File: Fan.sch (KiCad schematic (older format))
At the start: 9 parts

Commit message: Added Arduino and top-level connections
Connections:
- net labels added: CURR_MEAS, FAN_EN_N, FAN_OUT+, FAN_OUT-, TACH_IN, TACH_MEAS
- net labels removed: Current_Measure, Fan_in, Power+, Power-, Tach, Tach_out
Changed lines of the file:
@@
 $Descr A4 11693 8268
 encoding utf-8
-Sheet 7 9
+Sheet 8 9
 Title ""
 Date ""
@@
 $EndDescr
 Text HLabel 8800 3400 0    60   Output ~ 0
-Power+
-Text HLabel 8800 3600 0    60   Input ~ 0
-Power-
+FAN_OUT+
+Text HLabel 8800 3600 0    60   Output ~ 0
+FAN_OUT-
 Text HLabel 8800 4000 0    60   Input ~ 0
-Tach
+TACH_IN
 Text HLabel 1500 5300 0    60   Output ~ 0
-Tach_out
+TACH_MEAS
 Text HLabel 1500 4700 0    60   Input ~ 0
-Fan_in
+FAN_EN_N
 $Comp
 L LM324 U?
@@
 	7800 5300 1500 5300
 Text HLabel 1500 5000 0    60   Output ~ 0
-Current_Measure
+CURR_MEAS
 Wire Wire Line
 	7200 3900 6600 3900

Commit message: Current/fan driver circuit reworked
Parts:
- removed R? (x3): R, symbol R
- removed RV?: POT, symbol POT
- added D?: DIODE, symbol DIODE
- added Q? (x2): MOSFET_N, symbol MOSFET_N
- added TH?: THERMISTOR, symbol THERMISTOR
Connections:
- net labels added: +12C, FAN_MODE, FAN_PWM
- net labels removed: FAN_EN_N
- wire segments 36 -> 34
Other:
- moved on the sheet: R?
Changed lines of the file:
@@
 $Descr A4 11693 8268
 encoding utf-8
-Sheet 8 9
+Sheet 7 9
 Title ""
 Date ""
@@
 Comment4 ""
 $EndDescr
-Text HLabel 8800 3400 0    60   Output ~ 0
+Text HLabel 10500 1700 2    60   Output ~ 0
 FAN_OUT+
-Text HLabel 8800 3600 0    60   Output ~ 0
+Text HLabel 10500 1900 2    60   Output ~ 0
 FAN_OUT-
-Text HLabel 8800 4000 0    60   Input ~ 0
+Text HLabel 10500 6100 2    60   Input ~ 0
 TACH_IN
-Text HLabel 1500 5300 0    60   Output ~ 0
+Text HLabel 1500 6100 0    60   Output ~ 0
 TACH_MEAS
-Text HLabel 1500 4700 0    60   Input ~ 0
-FAN_EN_N
+Text HLabel 1500 3600 0    60   Input ~ 0
+FAN_PWM
 $Comp
 L LM324 U?
@@
 $EndComp
 $Comp
-L +12V #PWR?
-U 1 1 52F02708
-P 7200 2000
-F 0 "#PWR?" H 7200 1950 20  0001 C CNN
-F 1 "+12V" H 7200 2100 30  0000 C CNN
-F 2 "" H 7200 2000 60  0000 C CNN
-F 3 "" H 7200 2000 60  0000 C CNN
-	1    7200 2000
-	1    0    0    -1
-$EndComp
-Wire Wire Line
-	7200 2000 7200 2400
-Wire Wire Line
-	7200 2800 7200 3400
-Wire Wire Line
-	7200 3400 8800 3400
-Wire Wire Line
-	5100 3600 7200 3600
-Wire Wire Line
-	7200 3600 8800 3600
-Wire Wire Line
-	7200 3600 7200 3900
-Wire Wire Line
-	7200 3900 7200 4100
-$Comp
 L R R?
 U 1 1 52F02733
-P 7200 4350
-F 0 "R?" V 7280 4350 40  0000 C CNN
-F 1 "R" V 7207 4351 40  0000 C CNN
-F 2 "" V 7130 4350 30  0000 C CNN
-F 3 "" H 7200 4350 30  0000 C CNN
-	1    7200 4350
+P 7200 5050
+F 0 "R?" V 7280 5050 40  0000 C CNN
+F 1 "R" V 7207 5051 40  0000 C CNN
+F 2 "" V 7130 5050 30  0000 C CNN
+F 3 "" H 7200 5050 30  0000 C CNN
+	1    7200 5050
 	1    0    0    -1
 $EndComp
@@
 L AGND #PWR?
 U 1 1 52F02747
-P 7200 5000
-F 0 "#PWR?" H 7200 5000 40  0001 C CNN
-F 1 "AGND" H 7200 4930 50  0000 C CNN
-F 2 "" H 7200 5000 60  0000 C CNN
-F 3 "" H 7200 5000 60  0000 C CNN
-	1    7200 5000
-	1    0    0    -1
-$EndComp
-Wire Wire Line
-	7200 4600 7200 5000
-Wire Wire Line
-	6400 2600 6900 2600
+P 7200 5700
+F 0 "#PWR?" H 7200 5700 40  0001 C CNN
+F 1 "AGND" H 7200 5630 50  0000 C CNN
+F 2 "" H 7200 5700 60  0000 C CNN
+F 3 "" H 7200 5700 60  0000 C CNN
+	1    7200 5700
+	1    0    0    -1
+$EndComp
 $Comp
 L +12V #PWR?
@@
 	1    0    0    -1
 $EndComp
-Wire Wire Line
-	5800 1900 5800 2200
 $Comp
 L -12V #PWR?
@@
 	-1   0    0    1
 $EndComp
-Wire Wire Line
-	5800 3250 5800 3000
-Wire Wire Line
-	5100 3600 5100 2700
-Wire Wire Line
-	5100 2700 5400 2700
-Connection ~ 7200 3600
-Wire Wire Line
-	3600 2500 3900 2500
-Wire Wire Line
-	3900 2500 4400 2500
-Wire Wire Line
-	4400 2500 5400 2500
-$Comp
-L R R?
-U 1 1 52F027CA
-P 3900 2050
-F 0 "R?" V 3980 2050 40  0000 C CNN
-F 1 "R" V 3907 2051 40  0000 C CNN
-F 2 "" V 3830 2050 30  0000 C CNN
-F 3 "" H 3900 2050 30  0000 C CNN
-	1    3900 2050
-	1    0    0    -1
-$EndComp
-Wire Wire Line
-	3900 2300 3900 2500
-Wire Wire Line
-	3900 2500 3900 2900
-$Comp
-L +12V #PWR?
-U 1 1 52F027E4
-P 3900 1500
-F 0 "#PWR?" H 3900 1450 20  0001 C CNN
-F 1 "+12V" H 3900 1600 30  0000 C CNN
-F 2 "" H 3900 1500 60  0000 C CNN
-F 3 "" H 3900 1500 60  0000 C CNN
-	1    3900 1500
-	1    0    0    -1
-$EndComp
-Wire Wire Line
-	3900 1500 3900 1800
-$Comp
-L POT RV?
-U 1 1 52F02801
-P 3900 3150
-F 0 "RV?" H 3900 3050 50  0000 C CNN
-F 1 "POT" H 3900 3150 50  0000 C CNN
-F 2 "" H 3900 3150 60  0000 C CNN
-F 3 "" H 3900 3150 60  0000 C CNN
-	1    3900 3150
-	0    -1   -1   0
-$EndComp
-Connection ~ 3900 2500
 $Comp
 L AGND #PWR?
 U 1 1 52F0282F
-P 3900 3700
-F 0 "#PWR?" H 3900 3700 40  0001 C CNN
-F 1 "AGND" H 3900 3630 50  0000 C CNN
-F 2 "" H 3900 3700 60  0000 C CNN
-F 3 "" H 3900 3700 60  0000 C CNN
-	1    3900 3700
-	1    0    0    -1
-$EndComp
-Wire Wire Line
-	3900 3700 3900 3400
+P 4600 3400
+F 0 "#PWR?" H 4600 3400 40  0001 C CNN
+F 1 "AGND" H 4600 3330 50  0000 C CNN
+F 2 "" H 4600 3400 60  0000 C CNN
+F 3 "" H 4600 3400 60  0000 C CNN
+	1    4600 3400
+	1    0    0    -1
+$EndComp
 $Comp
 L MCP4922-E/P U?
@@
 	1    0    0    -1
 $EndComp
-Wire Wire Line
-	8800 4000 7800 4000
-Wire Wire Line
-	7800 4000 7800 5300
-Wire Wire Line
-	7800 5300 1500 5300
-Text HLabel 1500 5000 0    60   Output ~ 0
+Text HLabel 1500 4400 0    60   Output ~ 0
 CURR_MEAS
-Wire Wire Line
-	7200 3900 6600 3900
-Wire Wire Line
-	6600 3900 6600 5000
-Wire Wire Line
-	6600 5000 1500 5000
-Connection ~ 7200 3900
-$Comp
-L R R?
-U 1 1 52F0289B
-P 4400 3150
-F 0 "R?" V 4480 3150 40  0000 C CNN
-F 1 "R" V 4407 3151 40  0000 C CNN
-F 2 "" V 4330 3150 30  0000 C CNN
-F 3 "" H 4400 3150 30  0000 C CNN
-	1    4400 3150
-	1    0    0    -1
-$EndComp
-Wire Wire Line
-	4400 2900 4400 2500
-Connection ~ 4400 2500
-Wire Wire Line
-	4400 3400 4400 4700
-Wire Wire Line
-	4400 4700 1800 4700
-Wire Wire Line
-	1800 4700 1500 4700
 $Comp
 L R R?
@@
 Text HLabel 1500 2450 0    60   Input ~ 0
 MOSI
-Text HLabel 1500 3100 0    60   Output ~ 0
+Text HLabel 1450 2750 0    60   Output ~ 0
 MISO
 Text HLabel 1500 2650 0    60   Input ~ 0
@@
 Text HLabel 1500 2550 0    60   Input ~ 0
 SCLK
+$Comp
+L MOSFET_N Q?
+U 1 1 52FBE00D
+P 6600 5000
+F 0 "Q?" H 6610 5170 60  0000 R CNN
+F 1 "MOSFET_N" H 6610 4850 60  0000 R CNN
+F 2 "" H 6600 5000 60  0000 C CNN
+F 3 "" H 6600 5000 60  0000 C CNN
+	1    6600 5000
+	1    0    0    -1
+$EndComp
+$Comp
+L THERMISTOR TH?
+U 1 1 52FBE056
+P 7200 1050
+F 0 "TH?" V 7300 1100 50  0000 C CNN
+F 1 "THERMISTOR" V 7100 1050 50  0000 C CNN
+F 2 "" H 7200 1050 60  0000 C CNN
+F 3 "" H 7200 1050 60  0000 C CNN
+	1    7200 1050
+	1    0    0    -1
+$EndComp
+Wire Wire Line
+	7200 3600 5100 3600
+Wire Wire Line
+	7200 5300 7200 5700
+Wire Wire Line
+	6400 2600 6900 2600
+Wire Wire Line
+	5800 1900 5800 2200
+Wire Wire Line
+	5800 3250 5800 3000
+Wire Wire Line
+	5100 3600 5100 2700
+Wire Wire Line
+	5100 2700 5400 2700
+Connection ~ 7200 3600
+Wire Wire Line
+	3600 2500 5400 2500
+Wire Wire Line
+	4600 3400 4600 3100
+Wire Wire Line
+	7200 4400 1500 4400
 Wire Wire Line
 	1800 2450 1500 2450
@@
 Wire Wire Line
 	1800 2650 1500 2650
-$Comp
-L R R?
-U 1 1 52F029BB
-P 1800 3350
-F 0 "R?" V 1880 3350 40  0000 C CNN
-F 1 "R" V 1807 3351 40  0000 C CNN
-F 2 "" V 1730 3350 30  0000 C CNN
-F 3 "" H 1800 3350 30  0000 C CNN
-	1    1800 3350
-	1    0    0    -1
-$EndComp
-Wire Wire Line
-	1800 3100 1800 2850
 Wire Wire Line
 	2900 2500 3100 2500
 Wire Wire Line
-	1800 3600 1800 4700
-Connection ~ 1800 4700
+	7200 800  7200 700
+Wire Wire Line
+	7200 1700 10500 1700
+Wire Wire Line
+	10500 1900 7200 1900
+$Comp
+L DIODE D?
+U 1 1 52FBE14F
+P 7000 1800
+F 0 "D?" H 7000 1900 40  0000 C CNN
+F 1 "DIODE" H 7000 1700 40  0000 C CNN
+F 2 "" H 7000 1800 60  0000 C CNN
+F 3 "" H 7000 1800 60  0000 C CNN
+	1    7000 1800
+	0    -1   -1   0
+$EndComp
+Wire Wire Line
+	7200 1300 7200 1700
+Wire Wire Line
+	7200 1900 7200 2400
+Wire Wire Line
+	7200 2100 7000 2100
+Wire Wire Line
+	7000 2100 7000 2000
+Connection ~ 7200 2100
+Wire Wire Line
+	7000 1600 7000 1500
+Wire Wire Line
+	7000 1500 7200 1500
+Connection ~ 7200 1500
+Connection ~ 7200 4400
+Wire Wire Line
+	7200 2800 7200 4800
+Wire Wire Line
+	6700 4800 6700 4600
+Wire Wire Line
+	6700 4600 7200 4600
+Connection ~ 7200 4600
+Wire Wire Line
+	7200 5500 6700 5500
+Wire Wire Line
+	6700 5500 6700 5200
+Connection ~ 7200 5500
+Wire Wire Line
+	10500 6100 1500 6100
+$Comp
+L MOSFET_N Q?
+U 1 1 52FBE558
+P 4500 2900
+F 0 "Q?" H 4510 3070 60  0000 R CNN
+F 1 "MOSFET_N" H 4510 2750 60  0000 R CNN
+F 2 "" H 4500 2900 60  0000 C CNN
+F 3 "" H 4500 2900 60  0000 C CNN
+	1    4500 2900
+	1    0    0    -1
+$EndComp
+Wire Wire Line
+	4600 2700 4600 2500
+Connection ~ 4600 2500
+Wire Wire Line
+	1500 3600 3700 3600
+Wire Wire Line
+	3700 3600 3700 2900
+Wire Wire Line
+	3700 2900 4300 2900
+Text HLabel 1500 5000 0    60   Input ~ 0
+FAN_MODE
+Wire Wire Line
+	1500 5000 6400 5000
+$Comp
+L +12C #PWR?
+U 1 1 52FBEABF
+P 7200 700
+F 0 "#PWR?" H 7200 670 30  0001 C CNN
+F 1 "+12C" H 7200 810 40  0000 C CNN
+F 2 "" H 7200 700 60  0000 C CNN
+F 3 "" H 7200 700 60  0000 C CNN
+	1    7200 700
+	1    0    0    -1
+$EndComp
 $EndSCHEMATC

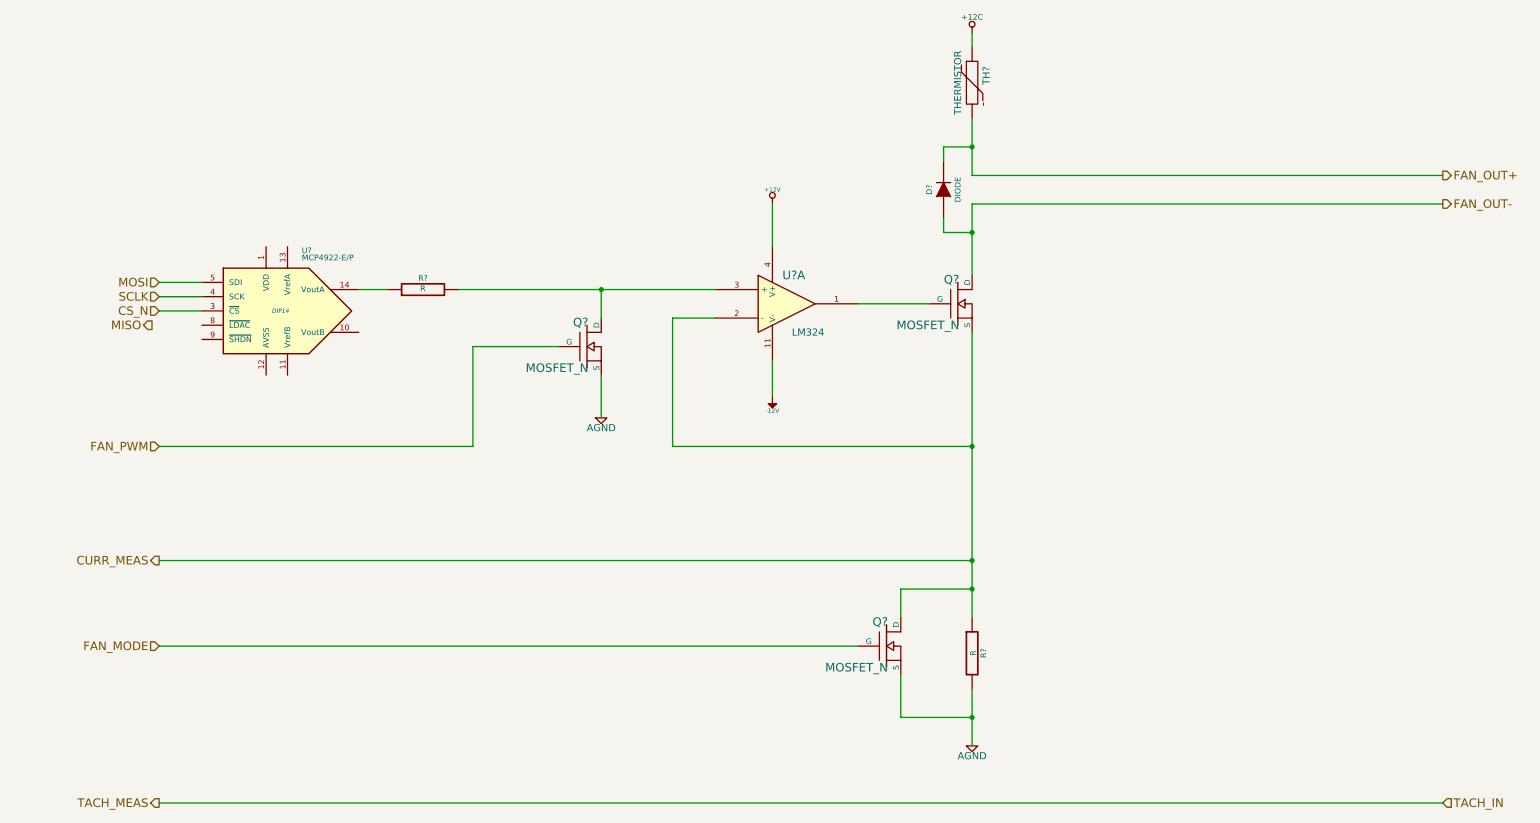
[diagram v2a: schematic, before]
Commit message: Added footprints for the relay module, preliminarily annotated schematic, relay components placed on PCB
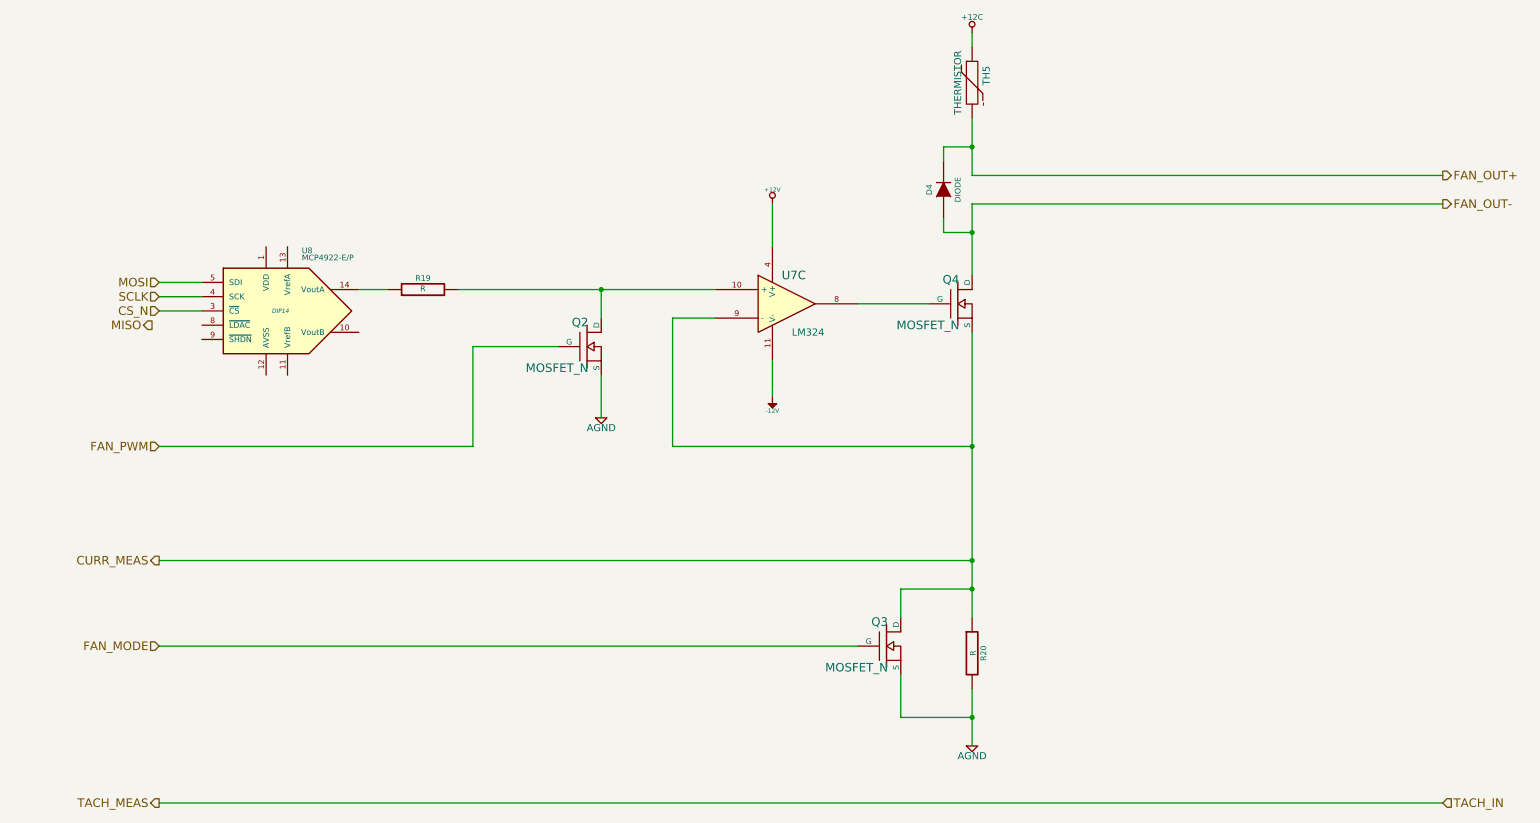
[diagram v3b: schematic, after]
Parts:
- gave numbers to parts that had none: 9
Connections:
- net CURR_MEAS: now also U7.9 (-); no longer U7.2 (-)
- net at Q4.G: now also U7.8; no longer U7.1
- net at Q2.D, R19.2: now also U7.10 (+); no longer U7.3 (+)
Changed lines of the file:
@@
 FAN_PWM
 $Comp
-L LM324 U?
-U 1 1 52F026D6
+L LM324 U7
+U 3 1 52F026D6
 P 5900 2600
-F 0 "U?" H 5950 2800 60  0000 C CNN
+F 0 "U7" H 5950 2800 60  0000 C CNN
 F 1 "LM324" H 6050 2400 50  0000 C CNN
 F 2 "" H 5900 2600 60  0000 C CNN
 F 3 "" H 5900 2600 60  0000 C CNN
-	1    5900 2600
-	1    0    0    -1
-$EndComp
-$Comp
-L MOSFET_N Q?
+	3    5900 2600
+	1    0    0    -1
+$EndComp
+$Comp
+L MOSFET_N Q4
 U 1 1 52F026F4
 P 7100 2600
-F 0 "Q?" H 7110 2770 60  0000 R CNN
+F 0 "Q4" H 7110 2770 60  0000 R CNN
 F 1 "MOSFET_N" H 7110 2450 60  0000 R CNN
 F 2 "" H 7100 2600 60  0000 C CNN
@@
 $EndComp
 $Comp
-L R R?
+L R R20
 U 1 1 52F02733
 P 7200 5050
-F 0 "R?" V 7280 5050 40  0000 C CNN
+F 0 "R20" V 7280 5050 40  0000 C CNN
 F 1 "R" V 7207 5051 40  0000 C CNN
 F 2 "" V 7130 5050 30  0000 C CNN
@@
 $EndComp
 $Comp
-L AGND #PWR?
+L AGND #PWR42
 U 1 1 52F02747
 P 7200 5700
-F 0 "#PWR?" H 7200 5700 40  0001 C CNN
+F 0 "#PWR42" H 7200 5700 40  0001 C CNN
 F 1 "AGND" H 7200 5630 50  0000 C CNN
 F 2 "" H 7200 5700 60  0000 C CNN
@@
 $EndComp
 $Comp
-L +12V #PWR?
+L +12V #PWR39
 U 1 1 52F02768
 P 5800 1900
-F 0 "#PWR?" H 5800 1850 20  0001 C CNN
+F 0 "#PWR39" H 5800 1850 20  0001 C CNN
 F 1 "+12V" H 5800 2000 30  0000 C CNN
 F 2 "" H 5800 1900 60  0000 C CNN
@@
 $EndComp
 $Comp
-L -12V #PWR?
+L -12V #PWR40
 U 1 1 52F02786
 P 5800 3250
-F 0 "#PWR?" H 5800 3380 20  0001 C CNN
+F 0 "#PWR40" H 5800 3380 20  0001 C CNN
 F 1 "-12V" H 5800 3350 30  0000 C CNN
 F 2 "" H 5800 3250 60  0000 C CNN
@@
 $EndComp
 $Comp
-L AGND #PWR?
+L AGND #PWR38
 U 1 1 52F0282F
 P 4600 3400
-F 0 "#PWR?" H 4600 3400 40  0001 C CNN
+F 0 "#PWR38" H 4600 3400 40  0001 C CNN
 F 1 "AGND" H 4600 3330 50  0000 C CNN
 F 2 "" H 4600 3400 60  0000 C CNN
@@
 $EndComp
 $Comp
-L MCP4922-E/P U?
+L MCP4922-E/P U8
 U 1 1 52F0284E
 P 2350 2650
-F 0 "U?" H 2500 3050 40  0000 L BNN
+F 0 "U8" H 2500 3050 40  0000 L BNN
 F 1 "MCP4922-E/P" H 2500 3000 40  0000 L BNN
 F 2 "DIP14" H 2350 2650 30  0000 C CIN
@@
 CURR_MEAS
 $Comp
-L R R?
+L R R19
 U 1 1 52F028DD
 P 3350 2500
-F 0 "R?" V 3430 2500 40  0000 C CNN
+F 0 "R19" V 3430 2500 40  0000 C CNN
 F 1 "R" V 3357 2501 40  0000 C CNN
 F 2 "" V 3280 2500 30  0000 C CNN
@@
 SCLK
 $Comp
-L MOSFET_N Q?
+L MOSFET_N Q3
 U 1 1 52FBE00D
 P 6600 5000
-F 0 "Q?" H 6610 5170 60  0000 R CNN
+F 0 "Q3" H 6610 5170 60  0000 R CNN
 F 1 "MOSFET_N" H 6610 4850 60  0000 R CNN
 F 2 "" H 6600 5000 60  0000 C CNN
@@
 $EndComp
 $Comp
-L THERMISTOR TH?
+L THERMISTOR TH5
 U 1 1 52FBE056
 P 7200 1050
-F 0 "TH?" V 7300 1100 50  0000 C CNN
+F 0 "TH5" V 7300 1100 50  0000 C CNN
 F 1 "THERMISTOR" V 7100 1050 50  0000 C CNN
 F 2 "" H 7200 1050 60  0000 C CNN
@@
 	10500 1900 7200 1900
 $Comp
-L DIODE D?
+L DIODE D4
 U 1 1 52FBE14F
 P 7000 1800
-F 0 "D?" H 7000 1900 40  0000 C CNN
+F 0 "D4" H 7000 1900 40  0000 C CNN
 F 1 "DIODE" H 7000 1700 40  0000 C CNN
 F 2 "" H 7000 1800 60  0000 C CNN
@@
 	10500 6100 1500 6100
 $Comp
-L MOSFET_N Q?
+L MOSFET_N Q2
 U 1 1 52FBE558
 P 4500 2900
-F 0 "Q?" H 4510 3070 60  0000 R CNN
+F 0 "Q2" H 4510 3070 60  0000 R CNN
 F 1 "MOSFET_N" H 4510 2750 60  0000 R CNN
 F 2 "" H 4500 2900 60  0000 C CNN
@@
 	1500 5000 6400 5000
 $Comp
-L +12C #PWR?
+L +12C #PWR41
 U 1 1 52FBEABF
 P 7200 700
-F 0 "#PWR?" H 7200 670 30  0001 C CNN
+F 0 "#PWR41" H 7200 670 30  0001 C CNN
 F 1 "+12C" H 7200 810 40  0000 C CNN
 F 2 "" H 7200 700 60  0000 C CNN

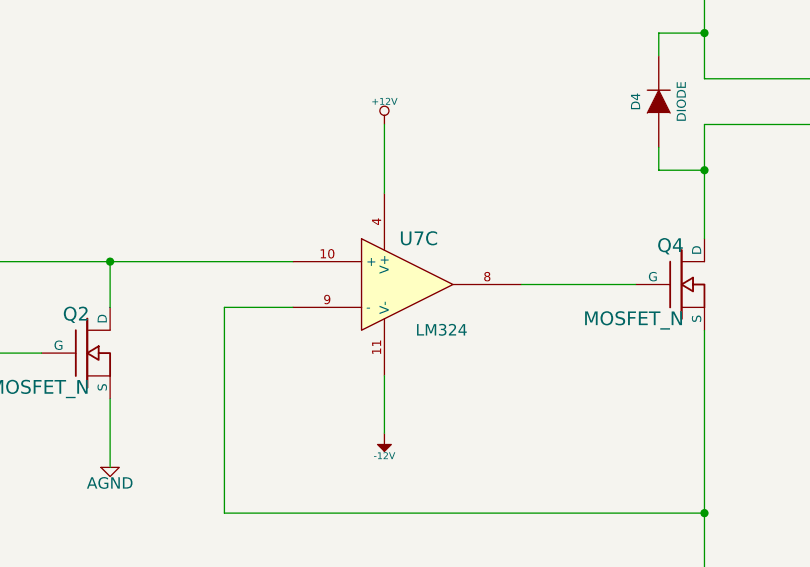
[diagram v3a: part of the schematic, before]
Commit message: Associated and placed the thermocouple module
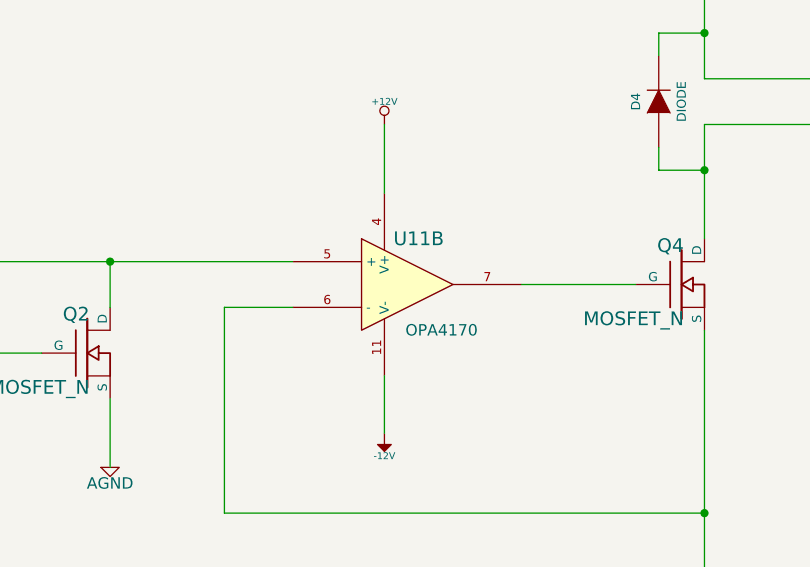
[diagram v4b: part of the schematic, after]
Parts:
- U11: renamed from U7; value LM324 -> OPA4170
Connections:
- net CURR_MEAS: now also U11.6 (-); no longer U11.9 (-)
- net at Q2.D, R19.2: now also U11.5 (+); no longer U11.10 (+)
- net at Q4.G: now also U11.7; no longer U11.8
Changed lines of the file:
@@
 FAN_PWM
 $Comp
-L LM324 U7
-U 3 1 52F026D6
+L LM324 U11
+U 2 1 52F026D6
 P 5900 2600
-F 0 "U7" H 5950 2800 60  0000 C CNN
-F 1 "LM324" H 6050 2400 50  0000 C CNN
+F 0 "U11" H 5950 2800 60  0000 C CNN
+F 1 "OPA4170" H 6050 2400 50  0000 C CNN
 F 2 "" H 5900 2600 60  0000 C CNN
 F 3 "" H 5900 2600 60  0000 C CNN
-	3    5900 2600
+	2    5900 2600
 	1    0    0    -1
 $EndComp
